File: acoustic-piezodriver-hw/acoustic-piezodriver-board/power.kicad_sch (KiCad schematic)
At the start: 69 parts, among them J2 Conn_02x04_Odd_Even, U1 LM3478MM, U10 NCE6005AS, U4 NCE6005AS, U5 LM3478MM, U8 NCE6005AS, U9 LM3478MM

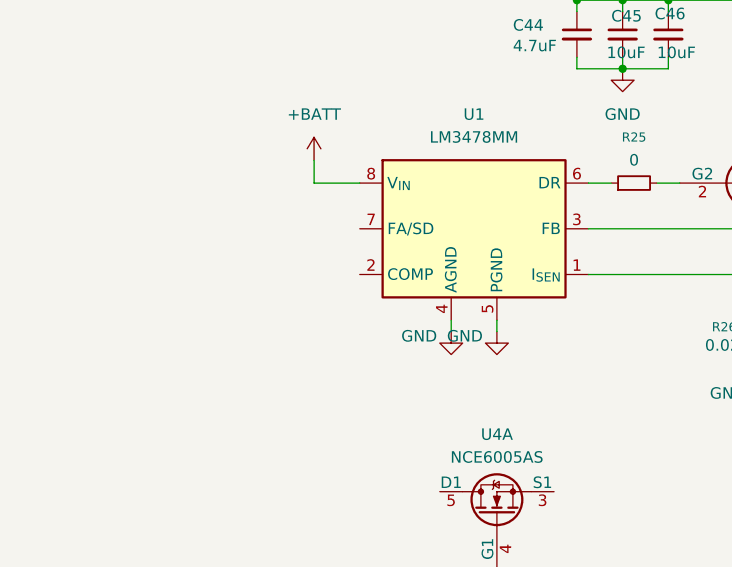
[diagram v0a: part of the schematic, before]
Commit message: [piezodriver] Finished boost converter dynamics, added compensation circuitry
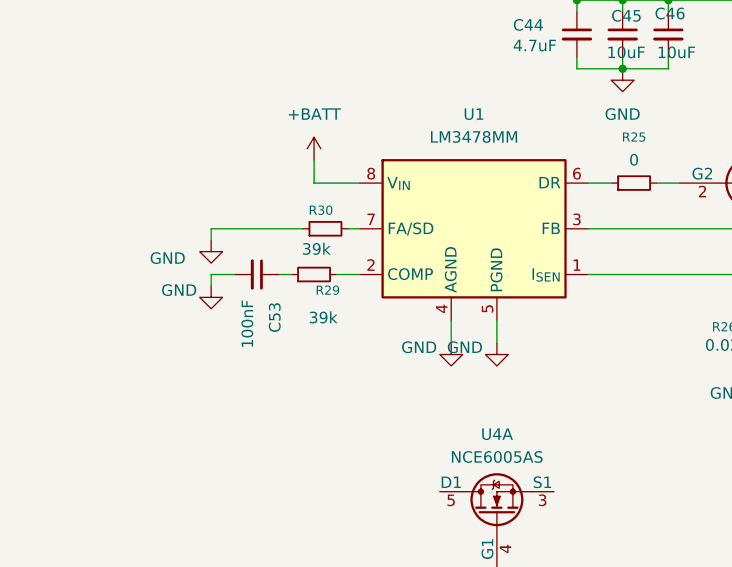
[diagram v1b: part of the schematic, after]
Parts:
- added C53: 100nF, Capacitor_SMD:C_0603_1608Metric, symbol Device:C_Small
- added R29, R30: 39k, Resistor_SMD:R_0603_1608Metric, symbol Device:R_Small
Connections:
- net GND: now also C53.2, R30.1
- net at U1.2 (COMP): now also R29.2
- net at U1.7 (FA/SD): now also R30.2
- new net: C53.1, R29.1

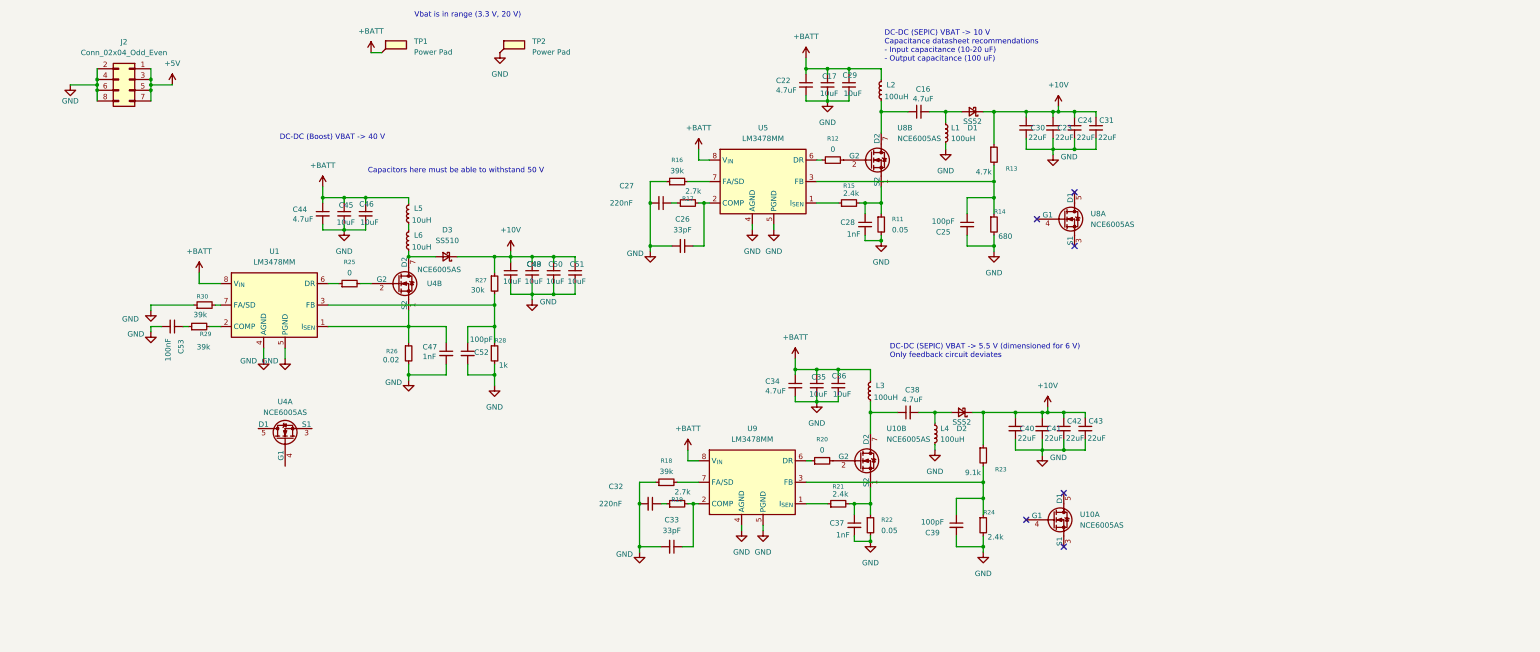
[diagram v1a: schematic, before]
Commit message: [carrier] Reordered carrier board (next) add magnetics to adc differential and ethernet instead of capacitors - SRF is too low
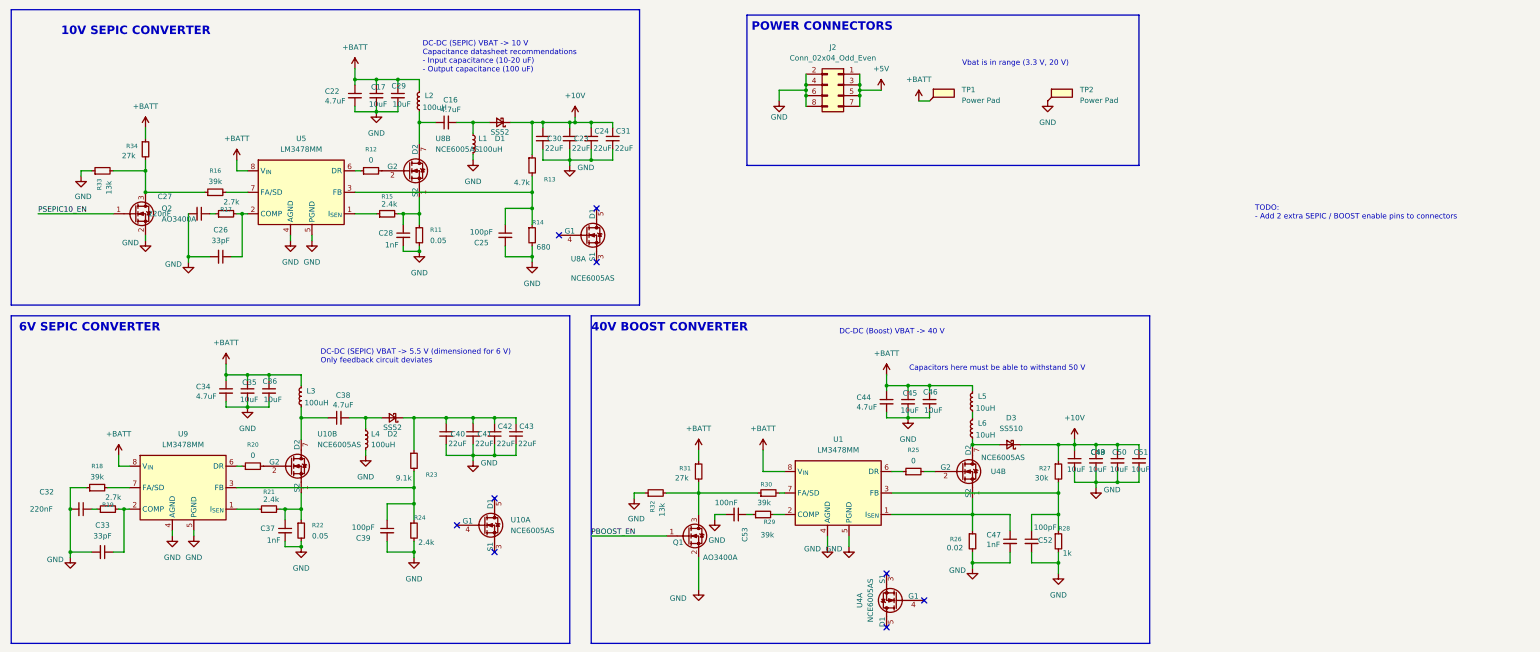
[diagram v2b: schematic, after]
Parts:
- added Q1, Q2: AO3400A, Package_TO_SOT_SMD:SOT-23, symbol Transistor_FET:AO3400A
- added R31, R34: 27k, Resistor_SMD:R_0603_1608Metric, symbol Device:R_Small
- added R32, R33: 13k, Resistor_SMD:R_0603_1608Metric, symbol Device:R_Small
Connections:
- net +10V: no longer C40.1, C41.1, C42.1, C43.1, D2.1 (K), R23.1
- net +BATT: now also R31.1, R34.1
- net GND: now also Q1.2 (S), Q2.2 (S), R32.1, R33.1; no longer R16.1, R30.1
- new net: C40.1, C41.1, C42.1, C43.1, D2.1 (K), R23.1
- new net: Q2.3 (D), R16.1, R33.2, R34.2
- new net: Q1.3 (D), R30.1, R31.2, R32.2
- new net PBOOST_EN: Q1.1 (G)
- new net PSEPIC10_EN: Q2.1 (G)
- no-connect marks 6 -> 9
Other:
- note added: "10V SEPIC CONVERTER"
- note added: "40V BOOST CONVERTER"
- note added: "6V SEPIC CONVERTER"
- note added: "POWER CONNECTORS"
- note added: "TODO: - Add 2 extra SEPIC / BOOST enable pins to connectors"
- moved on the sheet: C16, C17, C22, C23, C24, C25, C26, C27, C28, C29, C30, C31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

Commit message: [carrier] Research on piezo-element
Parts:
- added R35: 0, Resistor_SMD:R_0603_1608Metric_Pad0.98x0.95mm_HandSolder, symbol Device:R_Small
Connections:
- net at C47.1, R26.1, U4.1 (S2): now also R35.2; no longer U1.1 (I_{SEN})
- new net: R35.1, U1.1 (I_{SEN})
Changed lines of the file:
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@@
 	(wire
 		(pts
-			(xy 222.25 133.35) (xy 241.3 133.35)
+			(xy 222.25 133.35) (xy 224.79 133.35)
 		)
 		(stroke
@@
 		(pts
 			(xy 241.3 109.22) (xy 241.3 110.49)
+		)
+		(stroke
+			(width 0)
+			(type default)
+		)
+	)
+	(wire
+		(pts
+			(xy 229.87 133.35) (xy 241.3 133.35)
 		)
 		(stroke
@@
 					(unit 1)
 				)
+			)
+		)
+	)
+	(symbol
+		(lib_id "Device:R_Small")
+		(at 227.33 133.35 90)
+		(unit 1)
+		(exclude_from_sim no)
+		(in_bom yes)
+		(on_board yes)
+		(dnp no)
+		(fields_autoplaced yes)
+		(property "Reference" "R35"
+			(at 227.33 128.27 90)
+			(effects
+				(font
+					(size 1.016 1.016)
+				)
+			)
+		)
+		(property "Value" "0"
+			(at 227.33 130.81 90)
+			(effects
+				(font
+					(size 1.27 1.27)
+				)
+			)
+		)
+		(property "Footprint" "Resistor_SMD:R_0603_1608Metric_Pad0.98x0.95mm_HandSolder"
+			(at 227.33 133.35 0)
+			(effects
+				(font
+					(size 1.27 1.27)
+				)
+				(hide yes)
+			)
+		)
+		(property "Datasheet" "https://jlcpcb.com/api/file/downloadByFileSystemAccessId/8588882001185148928"
+			(at 227.33 133.35 0)
+			(effects
+				(font
+					(size 1.27 1.27)
+				)
+				(hide yes)
+			)
+		)
+		(property "Description" "100mW, change to damping resistor"
+			(at 227.33 133.35 0)
+			(effects
+				(font
+					(size 1.27 1.27)
+				)
+				(hide yes)
+			)
+		)
+		(property "LPN" "C15402"
+			(at 227.33 133.35 90)
+			(effects
+				(font
+					(size 1.27 1.27)
+				)
+				(hide yes)
+			)
+		)
+		(property "MPN" "0603WAJ0000T5E"
+			(at 227.33 133.35 90)
+			(effects
+				(font
+					(size 1.27 1.27)
+				)
+				(hide yes)
+			)
+		)
+		(pin "1"
+		)
+		(pin "2"
+		)
+		(instances
+			(project "acoustic-piezodriver-board"
+				(path "/94cb090f-214e-44cc-b8ed-ae50ff29d2bf/a0fbc78d-8163-4e6b-8d81-98a3dd6573cb"
+					(reference "R35")
+					(unit 1)
+				)

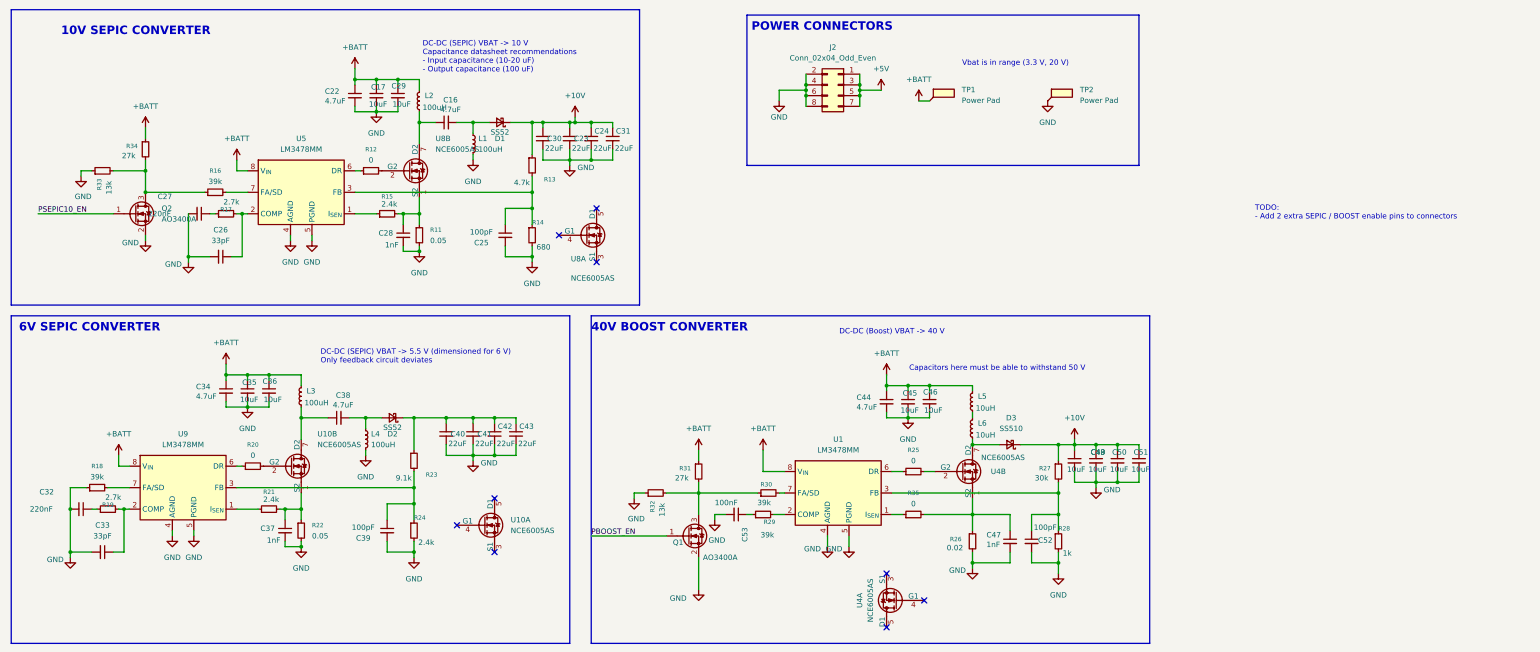
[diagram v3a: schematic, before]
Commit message: [carrier] Added second adc input with magnetics, added ethernet connector with magnetics [piezodriver] Added diodes to level shifters for gate charge return current
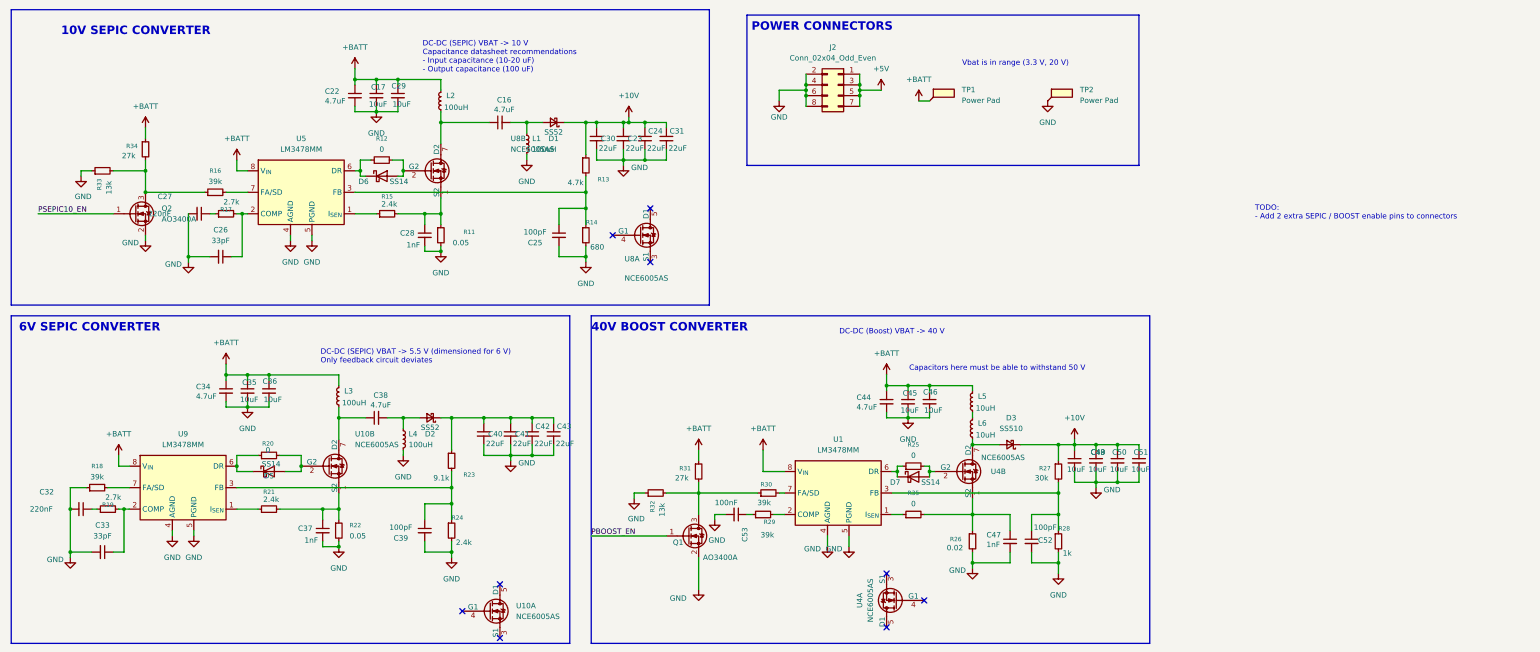
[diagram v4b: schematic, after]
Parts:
- added D5, D6, D7: SS14, Diode_SMD:D_SMA, symbol Diode:SS14
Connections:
- net at R12.1, U5.6 (DR): now also D6.1 (K)
- net at R12.2, U8.2 (G2): now also D6.2 (A)
- net at R25.1, U1.6 (DR): now also D7.1 (K)
- net at R25.2, U4.2 (G2): now also D7.2 (A)
- net at R20.1, U9.6 (DR): now also D5.1 (K)
- net at R20.2, U10.2 (G2): now also D5.2 (A)
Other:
- moved on the sheet: C16, C23, C24, C25, C28, C30, C31, C37, C38, C39, C40, C41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

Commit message: [piezodriver] Added temperature sensors + ldo + 8x2 connectors to carrier board
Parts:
- removed J2: Conn_02x04_Odd_Even, Connector_PinHeader_2.54mm:PinHeader_2x04_P2.54mm_Horizontal, symbol Connector_Generic:Conn_02x04_Odd_Even
- added J2: Conn_02x08_Odd_Even, Connector_PinHeader_2.54mm:PinHeader_2x08_P2.54mm_Horizontal, symbol Connector_Generic:Conn_02x08_Odd_Even
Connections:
- net +5V: now also J2.10 (Pin_10), J2.12 (Pin_12), J2.14 (Pin_14), J2.16 (Pin_16), J2.2 (Pin_2), J2.4 (Pin_4), J2.6 (Pin_6), J2.8 (Pin_8)
- net GND: now also J2.1 (Pin_1), J2.11 (Pin_11), J2.13 (Pin_13), J2.15 (Pin_15), J2.3 (Pin_3), J2.5 (Pin_5), J2.7 (Pin_7), J2.9 (Pin_9)
- net +6V: now reaches C40.1, C41.1, C42.1, C43.1, D2.1 (K), R23.1
- net PSEPIC10_EN renamed PSEPIC_EN
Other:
- moved on the sheet: C27

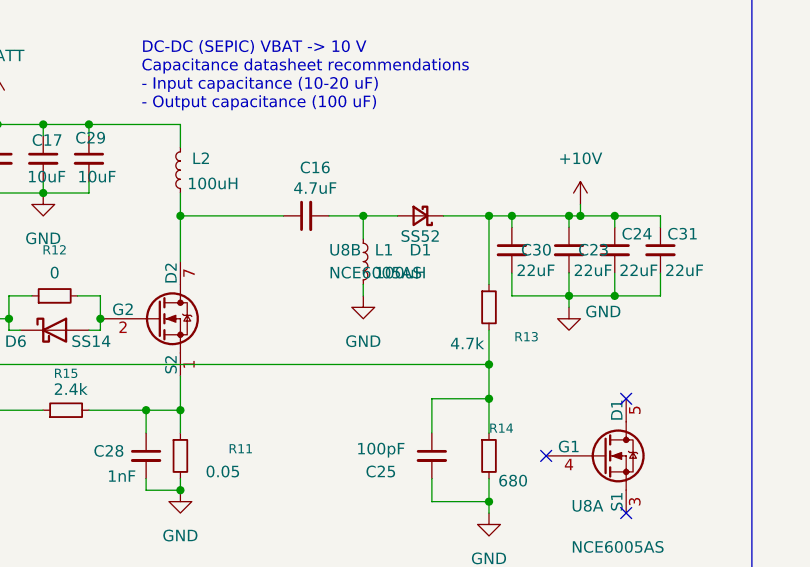
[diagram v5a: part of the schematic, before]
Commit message: [piezodriver] Added tina-ti simulation of 10V sepic (next) fix this sim, add power circuitry sim for carrier in tina-ti
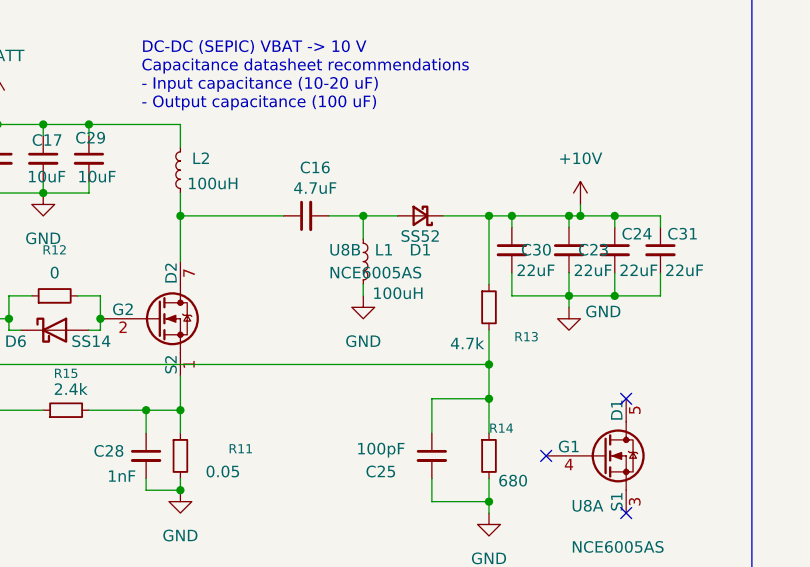
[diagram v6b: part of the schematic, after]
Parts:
- U10, U4, U8: footprint (none) -> Package_SO:SOP-8-1EP_4.57x4.57mm_P1.27mm_EP4.57x4.45mm_ThermalVias; LPN (none) -> C126151
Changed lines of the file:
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@@
 			)
 		)
-		(property "Footprint" ""
+		(property "Footprint" "Package_SO:SOP-8-1EP_4.57x4.57mm_P1.27mm_EP4.57x4.45mm_ThermalVias"
 			(at 217.17 153.67 0)
 			(effects
@@
 			)
 		)
-		(property "Datasheet" ""
+		(property "Datasheet" "https://jlcpcb.com/api/file/downloadByFileSystemAccessId/8588881119395647488"
 			(at 217.17 153.67 0)
 			(effects
@@
 			)
 		)
+		(property "LPN" "C126151"
+			(at 220.98 153.67 0)
+			(effects
+				(font
+					(size 1.27 1.27)
+				)
+				(hide yes)
+			)
+		)
 		(pin "6"
 		)
@@
 			)
 		)
-		(property "Footprint" ""
+		(property "Footprint" "Package_SO:SOP-8-1EP_4.57x4.57mm_P1.27mm_EP4.57x4.45mm_ThermalVias"
 			(at 168.91 67.31 0)
 			(effects
@@
 			)
 		)
-		(property "Datasheet" ""
+		(property "Datasheet" "https://jlcpcb.com/api/file/downloadByFileSystemAccessId/8588881119395647488"
 			(at 168.91 67.31 0)
 			(effects
@@
 			)
 		)
+		(property "LPN" "C126151"
+			(at 165.1 67.31 0)
+			(effects
+				(font
+					(size 1.27 1.27)
+				)
+				(hide yes)
+			)
+		)
 		(pin "6"
 		)
@@
 			)
 		)
-		(property "Footprint" ""
+		(property "Footprint" "Package_SO:SOP-8-1EP_4.57x4.57mm_P1.27mm_EP4.57x4.45mm_ThermalVias"
 			(at 95.25 121.92 0)
 			(effects
@@
 			)
 		)
-		(property "Datasheet" ""
+		(property "Datasheet" "https://jlcpcb.com/api/file/downloadByFileSystemAccessId/8588881119395647488"
 			(at 95.25 121.92 0)
 			(effects
@@
 			)
 		)
+		(property "LPN" "C126151"
+			(at 91.44 121.92 0)
+			(effects
+				(font
+					(size 1.27 1.27)
+				)
+				(hide yes)
+			)
+		)
 		(pin "6"
 		)
@@
 			)
 		)
-		(property "Footprint" ""
+		(property "Footprint" "Package_SO:SOP-8-1EP_4.57x4.57mm_P1.27mm_EP4.57x4.45mm_ThermalVias"
 			(at 119.38 52.07 0)
 			(effects
@@
 			)
 		)
-		(property "Datasheet" ""
+		(property "Datasheet" "https://jlcpcb.com/api/file/downloadByFileSystemAccessId/8588881119395647488"
 			(at 119.38 52.07 0)
 			(effects
@@
 			)
 		)
+		(property "LPN" "C126151"
+			(at 115.57 52.07 0)
+			(effects
+				(font
+					(size 1.27 1.27)
+				)
+				(hide yes)
+			)
+		)
 		(pin "6"
 		)
@@
 			)
 		)
-		(property "Footprint" ""
+		(property "Footprint" "Package_SO:SOP-8-1EP_4.57x4.57mm_P1.27mm_EP4.57x4.45mm_ThermalVias"
 			(at 133.35 156.21 0)
 			(effects
@@
 			)
 		)
-		(property "Datasheet" ""
+		(property "Datasheet" "https://jlcpcb.com/api/file/downloadByFileSystemAccessId/8588881119395647488"
 			(at 133.35 156.21 0)
 			(effects
@@
 			)
 		)
+		(property "LPN" "C126151"
+			(at 129.54 156.21 0)
+			(effects
+				(font
+					(size 1.27 1.27)
+				)
+				(hide yes)
+			)
+		)
 		(pin "6"
 		)
@@
 		(on_board yes)
 		(dnp no)
-		(fields_autoplaced yes)
 		(property "Reference" "L1"
 			(at 137.16 44.4499 0)
@@
 		)
 		(property "Value" "100uH"
-			(at 137.16 46.9899 0)
+			(at 136.906 49.276 0)
 			(effects
 				(font
@@
 			)
 		)
-		(property "Footprint" ""
+		(property "Footprint" "Package_SO:SOP-8-1EP_4.57x4.57mm_P1.27mm_EP4.57x4.45mm_ThermalVias"
 			(at 245.11 123.19 0)
 			(effects
@@
 			)
 		)
-		(property "Datasheet" ""
+		(property "Datasheet" "https://jlcpcb.com/api/file/downloadByFileSystemAccessId/8588881119395647488"
 			(at 245.11 123.19 0)
 			(effects
@@
 			(at 241.3 123.19 0)
 			(effects
+				(font
+					(size 1.27 1.27)
+				)
+				(hide yes)
+			)
+		)
+		(property "LPN" "C126151"
+			(at 241.3 123.19 0)
+			(effects
